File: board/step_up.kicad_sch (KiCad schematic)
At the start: 6 parts

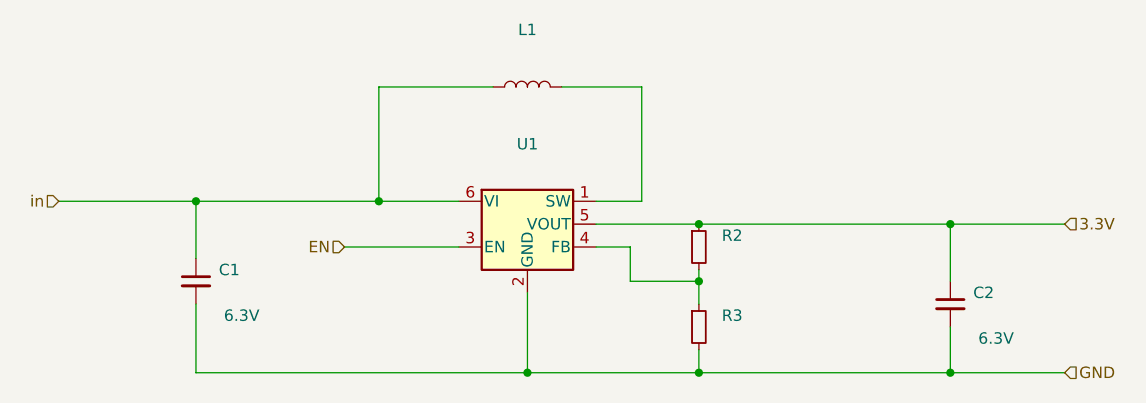
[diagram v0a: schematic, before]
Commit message: moved components for better EMC
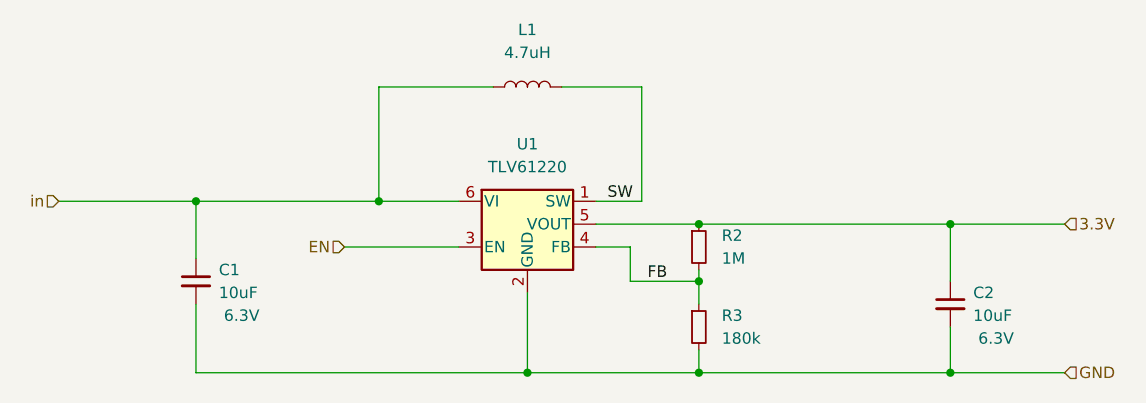
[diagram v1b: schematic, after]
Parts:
- C1, C2: value (none) -> 10uF; footprint (none) -> Capacitor_SMD:C_0603_1608Metric
- L1: value (none) -> 4.7uH; footprint (none) -> Inductor_SMD:L_0805_2012Metric
- R2: value (none) -> 1M; footprint (none) -> Resistor_SMD:R_0603_1608Metric
- R3: value (none) -> 180k; footprint (none) -> Resistor_SMD:R_0603_1608Metric
- U1: value (none) -> TLV61220; footprint (none) -> Package_TO_SOT_SMD:SOT-23-6
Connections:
- net FB: now reaches R2.2, R3.1, U1.4 (FB)
- net SW: now reaches L1.2, U1.1 (SW)
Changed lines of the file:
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@@
     (stroke (width 0) (type default) (color 0 0 0 0))
+  )
+  (label "SW" (at 147.32 109.22 0)
+    (effects (font (size 1.27 1.27)) (justify left bottom))
+  )
+  (label "FB" (at 151.765 118.11 0)
+    (effects (font (size 1.27 1.27)) (justify left bottom))
   )
   (hierarchical_label "EN" (shape input) (at 118.11 114.3 180)
@@
       (effects (font (size 1.27 1.27)) (justify left))
     )
-    (property "Value" "" (id 1) (at 160.02 124.4599 0)
+    (property "Value" "180k" (id 1) (at 160.02 124.4599 0)
       (effects (font (size 1.27 1.27)) (justify left))
     )
-    (property "Footprint" "" (id 2) (at 157.48 123.19 0)
+    (property "Footprint" "Resistor_SMD:R_0603_1608Metric" (id 2) (at 157.48 123.19 0)
       (effects (font (size 1.27 1.27)) hide)
     )
@@
       (effects (font (size 1.27 1.27)) (justify left))
     )
-    (property "Value" "" (id 1) (at 187.96 121.9262 0)
+    (property "Value" "10uF" (id 1) (at 187.96 121.9262 0)
       (effects (font (size 1.27 1.27)) (justify left))
     )
-    (property "Footprint" "" (id 2) (at 185.42 120.65 0)
+    (property "Footprint" "Capacitor_SMD:C_0603_1608Metric" (id 2) (at 185.42 120.65 0)
       (effects (font (size 1.27 1.27)) hide)
     )
@@
       (effects (font (size 1.27 1.27)) (justify left))
     )
-    (property "Value" "" (id 1) (at 160.02 115.5699 0)
+    (property "Value" "1M" (id 1) (at 160.02 115.5699 0)
       (effects (font (size 1.27 1.27)) (justify left))
     )
-    (property "Footprint" "" (id 2) (at 157.48 114.3 0)
+    (property "Footprint" "Resistor_SMD:R_0603_1608Metric" (id 2) (at 157.48 114.3 0)
       (effects (font (size 1.27 1.27)) hide)
     )
@@
       (effects (font (size 1.27 1.27)) (justify left))
     )
-    (property "Value" "" (id 1) (at 104.14 119.3862 0)
+    (property "Value" "10uF" (id 1) (at 104.14 119.3862 0)
       (effects (font (size 1.27 1.27)) (justify left))
     )
-    (property "Footprint" "" (id 2) (at 101.6 118.11 0)
+    (property "Footprint" "Capacitor_SMD:C_0603_1608Metric" (id 2) (at 101.6 118.11 0)
       (effects (font (size 1.27 1.27)) hide)
     )
@@
     (in_bom yes) (on_board yes) (fields_autoplaced)
     (property "Reference" "L1" (id 0) (at 138.43 90.17 90))
-    (property "Value" "" (id 1) (at 138.43 92.71 90))
-    (property "Footprint" "" (id 2) (at 138.43 96.52 0)
+    (property "Value" "4.7uH" (id 1) (at 138.43 92.71 90))
+    (property "Footprint" "Inductor_SMD:L_0805_2012Metric" (id 2) (at 138.43 96.52 0)
       (effects (font (size 1.27 1.27)) hide)
     )
@@
     (in_bom yes) (on_board yes) (fields_autoplaced)
     (property "Reference" "U1" (id 0) (at 138.43 102.87 0))
-    (property "Value" "" (id 1) (at 138.43 105.41 0))
-    (property "Footprint" "" (id 2) (at 139.7 118.11 0)
+    (property "Value" "TLV61220" (id 1) (at 138.43 105.41 0))
+    (property "Footprint" "Package_TO_SOT_SMD:SOT-23-6" (id 2) (at 139.7 118.11 0)
       (effects (font (size 1.27 1.27) italic) (justify left) hide)
     )
